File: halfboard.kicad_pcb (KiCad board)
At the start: 2 copper layers, 117.4 x 87.9 mm, 54 parts, among them U1 

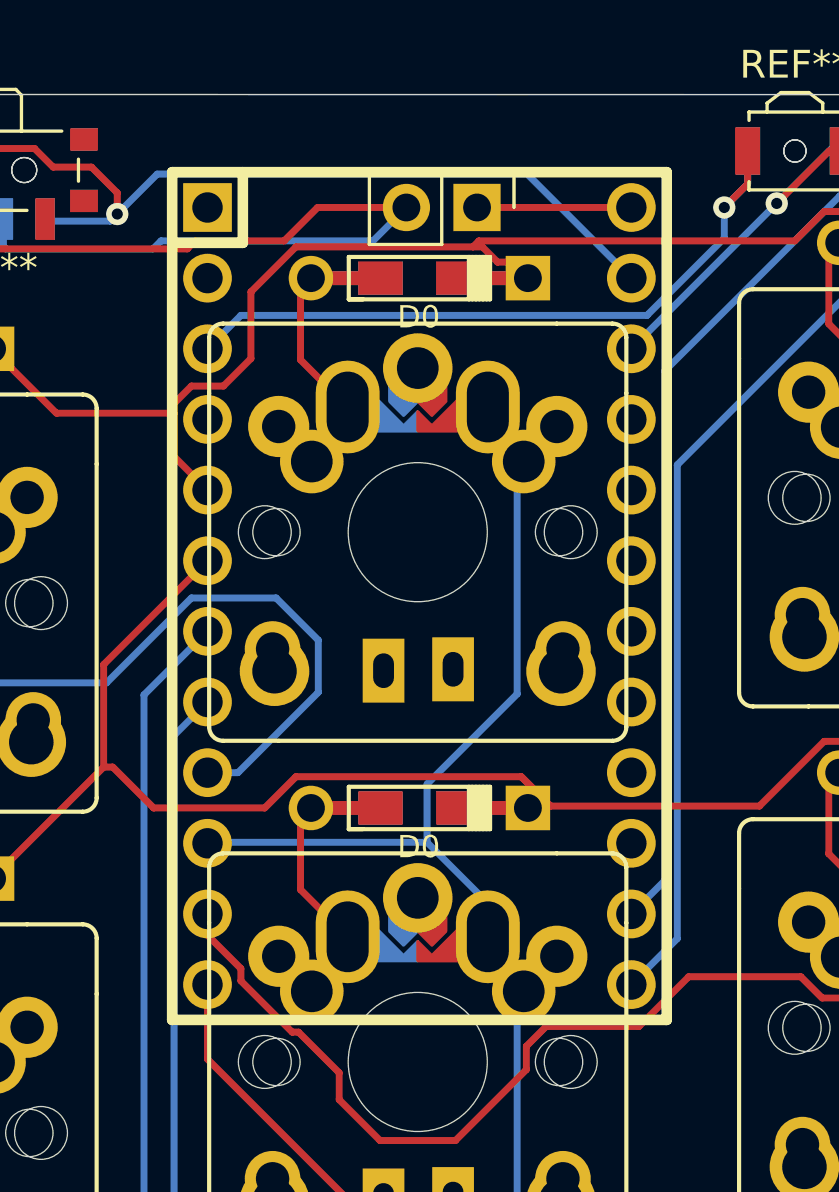
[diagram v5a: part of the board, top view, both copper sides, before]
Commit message: remove some unneeded silkscreen
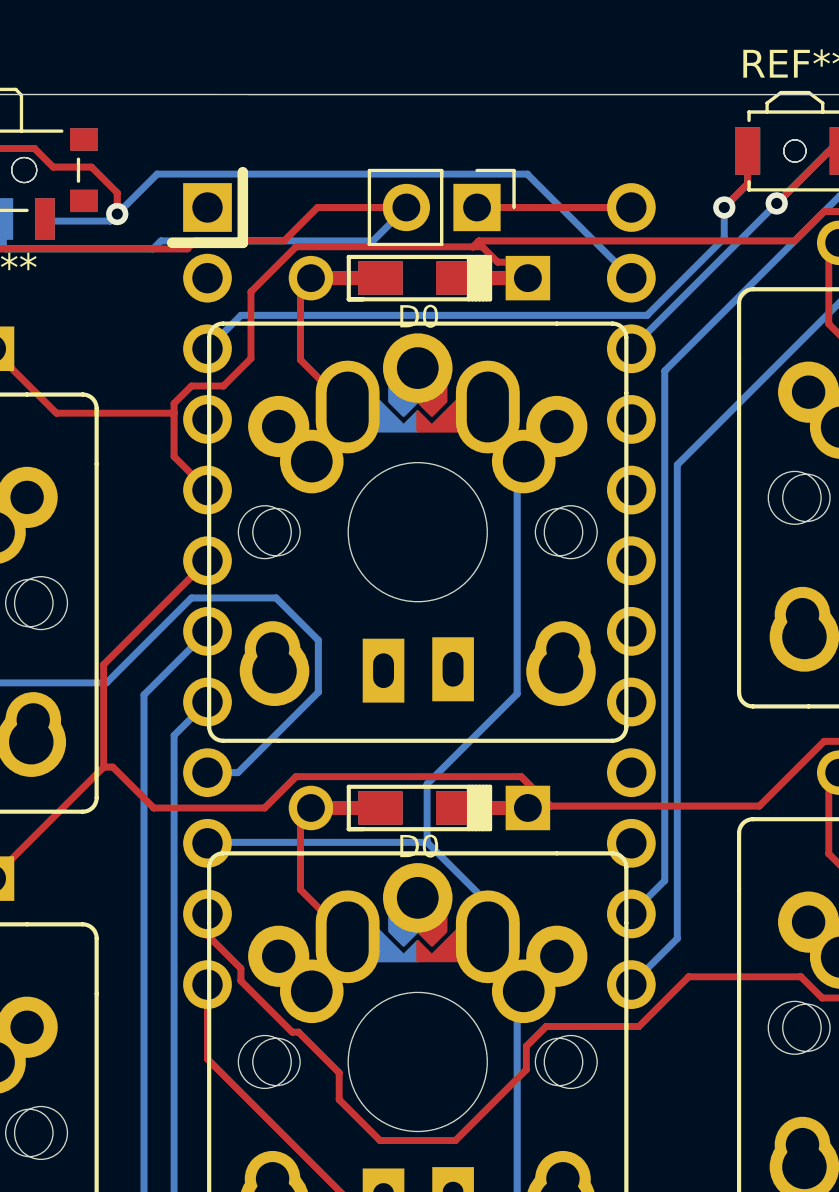
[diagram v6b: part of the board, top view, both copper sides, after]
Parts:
- removed the REF** at (52.6, 48.5) (x2)
- added  : SW_SPDT_PCM12, Button_Switch_SMD:SW_SPDT_PCM12, B.Cu at (52.6, 48.5)
- added REF**: SW_SPDT_PCM12, Button_Switch_SMD:SW_SPDT_PCM12, F.Cu at (52.6, 48.5)
- REF**: value MX/ALPs/PG1350 -> (none)
- REF**: value SW_SPST_B3U-3000P-B -> (none)
- U1: footprint mlp:ArduinoProMicro-TopSide -> halfboard:ArduinoProMicro-TopSide

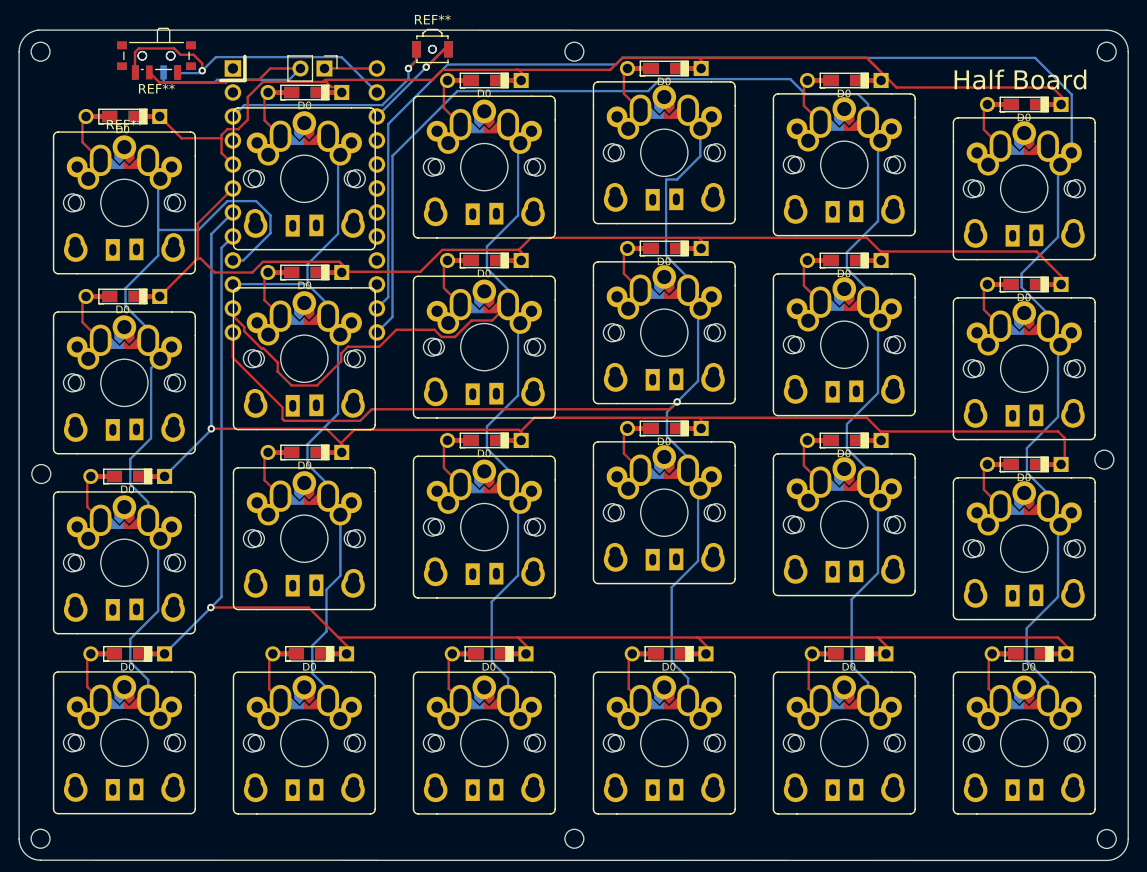
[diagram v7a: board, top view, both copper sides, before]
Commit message: rotated the switch footprint
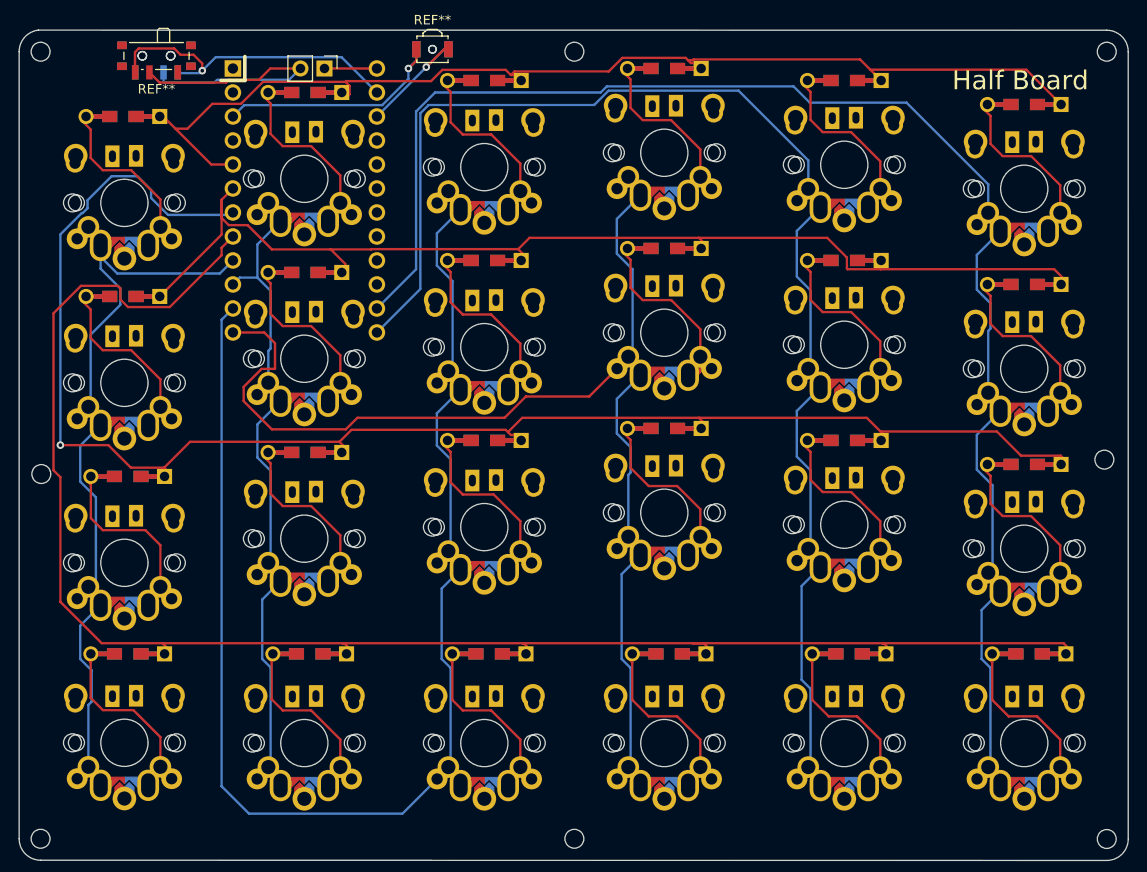
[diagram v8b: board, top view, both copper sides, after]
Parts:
- removed D0 (x22): D, mlp:Diode-dual
- added  : D, halfboard:Diode-dual, F.Cu at (144.4, 53.3)
- added  : D, halfboard:Diode-dual, F.Cu at (125.4, 50.8)
- added  : D, halfboard:Diode-dual, F.Cu at (106.3, 49.5)
- added  : D, halfboard:Diode-dual, F.Cu at (106.3, 68.6)
- added  : D, halfboard:Diode-dual, F.Cu at (106.3, 87.6)
- added  : D, halfboard:Diode-dual, F.Cu at (87.3, 88.9)
- added  : D, halfboard:Diode-dual, F.Cu at (87.3, 69.8)
- added  : , halfboard:Diode-dual, F.Cu at (87.3, 50.8)
- added  : , halfboard:Diode-dual, F.Cu at (68.3, 52.1)
- added  : , halfboard:Diode-dual, F.Cu at (68.3, 71.1)
- added  : D, halfboard:Diode-dual, F.Cu at (68.3, 90.2)
- added  : D, halfboard:Diode-dual, F.Cu at (144.4, 72.4)
- added  : D, halfboard:Diode-dual, F.Cu at (68.8, 111.5)
- added  : D, halfboard:Diode-dual, F.Cu at (49.5, 111.5)
- added  : D, halfboard:Diode-dual, F.Cu at (49.5, 92.7)
- added  : D, halfboard:Diode-dual, F.Cu at (144.4, 91.4)
- added  : D, halfboard:Diode-dual, F.Cu at (144.9, 111.5)
- added  : D, halfboard:Diode-dual, F.Cu at (125.9, 111.5)
- added  : D, halfboard:Diode-dual, F.Cu at (106.8, 111.5)
- added  : D, halfboard:Diode-dual, F.Cu at (87.8, 111.5)
- added  : D, halfboard:Diode-dual, F.Cu at (125.4, 88.9)
- added  : D, halfboard:Diode-dual, F.Cu at (125.4, 69.8)
-  : renamed from D0; value D -> (none); footprint mlp:Diode-dual -> halfboard:Diode-dual (x2)
-  : renamed from REF**
- turned   to 180 degrees (x15)
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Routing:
- net col2: track 100.3 -> 153.6 mm
- net row2: track 131.5 -> 165.4 mm
- net row3: track 150.3 -> 175.1 mm, vias 1 -> 0
- net col3: track 118.1 -> 135.2 mm, vias 1 -> 0
- net col0_row1: track 5.44 -> 22.1 mm
- net col0_row2: track 5.23 -> 21.8 mm
- net col3_row1: track 5.15 -> 21.4 mm
- net col2_row1: track 5.40 -> 21.4 mm
- net col2_row2: track 5.40 -> 21.2 mm
- net col0_row3: track 5.50 -> 21.3 mm
- net col5_row0: track 5.15 -> 20.8 mm
- net col4_row2: track 5.15 -> 20.8 mm
- net col4_row1: track 5.15 -> 20.8 mm
- net col5_row1: track 5.15 -> 20.8 mm
- net col5_row2: track 5.15 -> 20.8 mm
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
